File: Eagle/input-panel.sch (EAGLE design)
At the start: 23 parts, among them J1 UJC-HP-3-SMT-TR

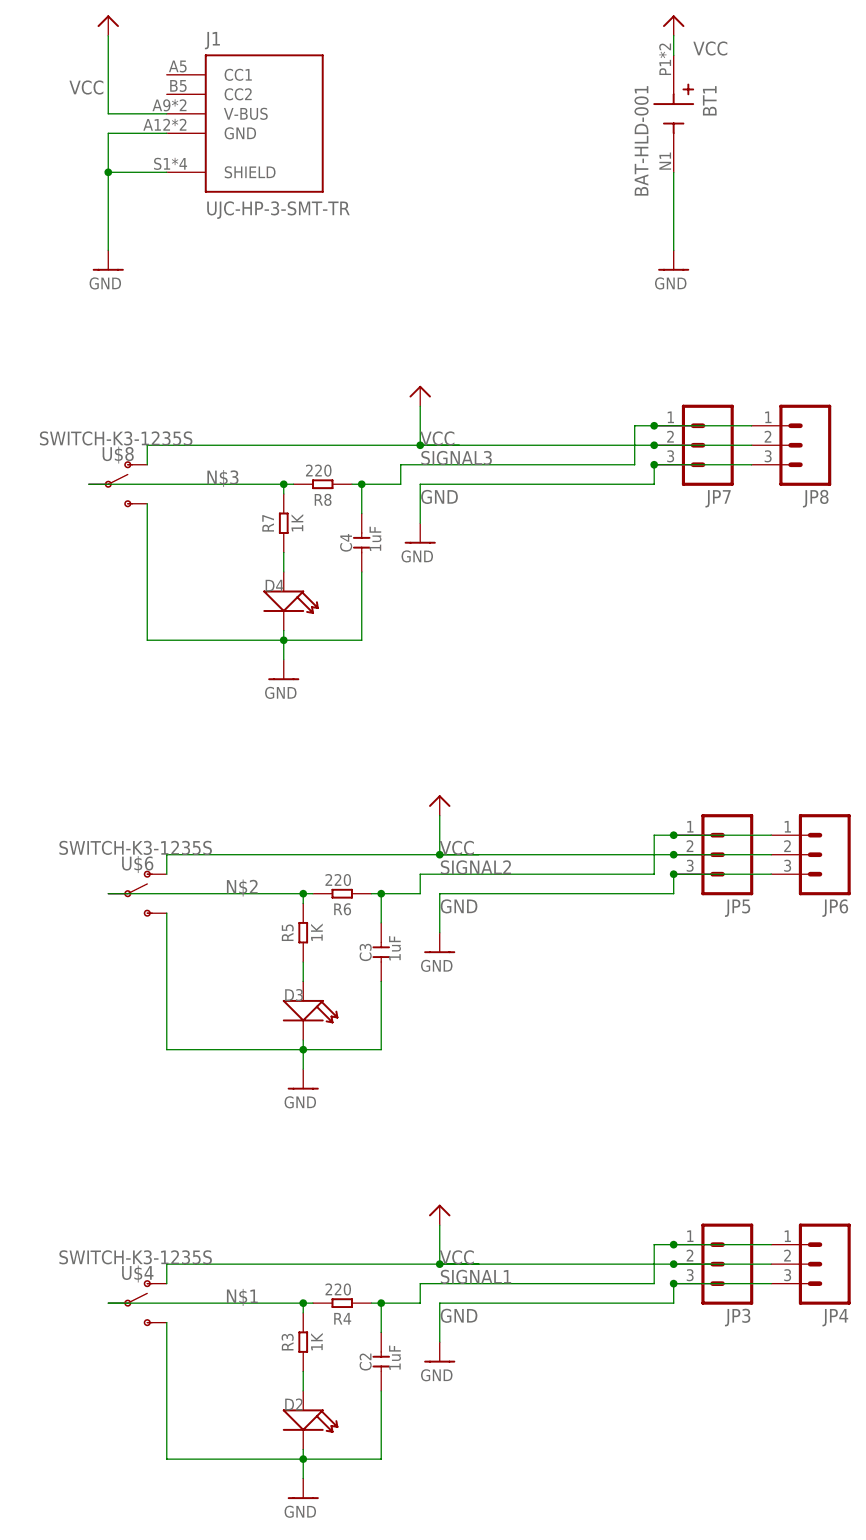
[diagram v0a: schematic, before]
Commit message: updated input panel
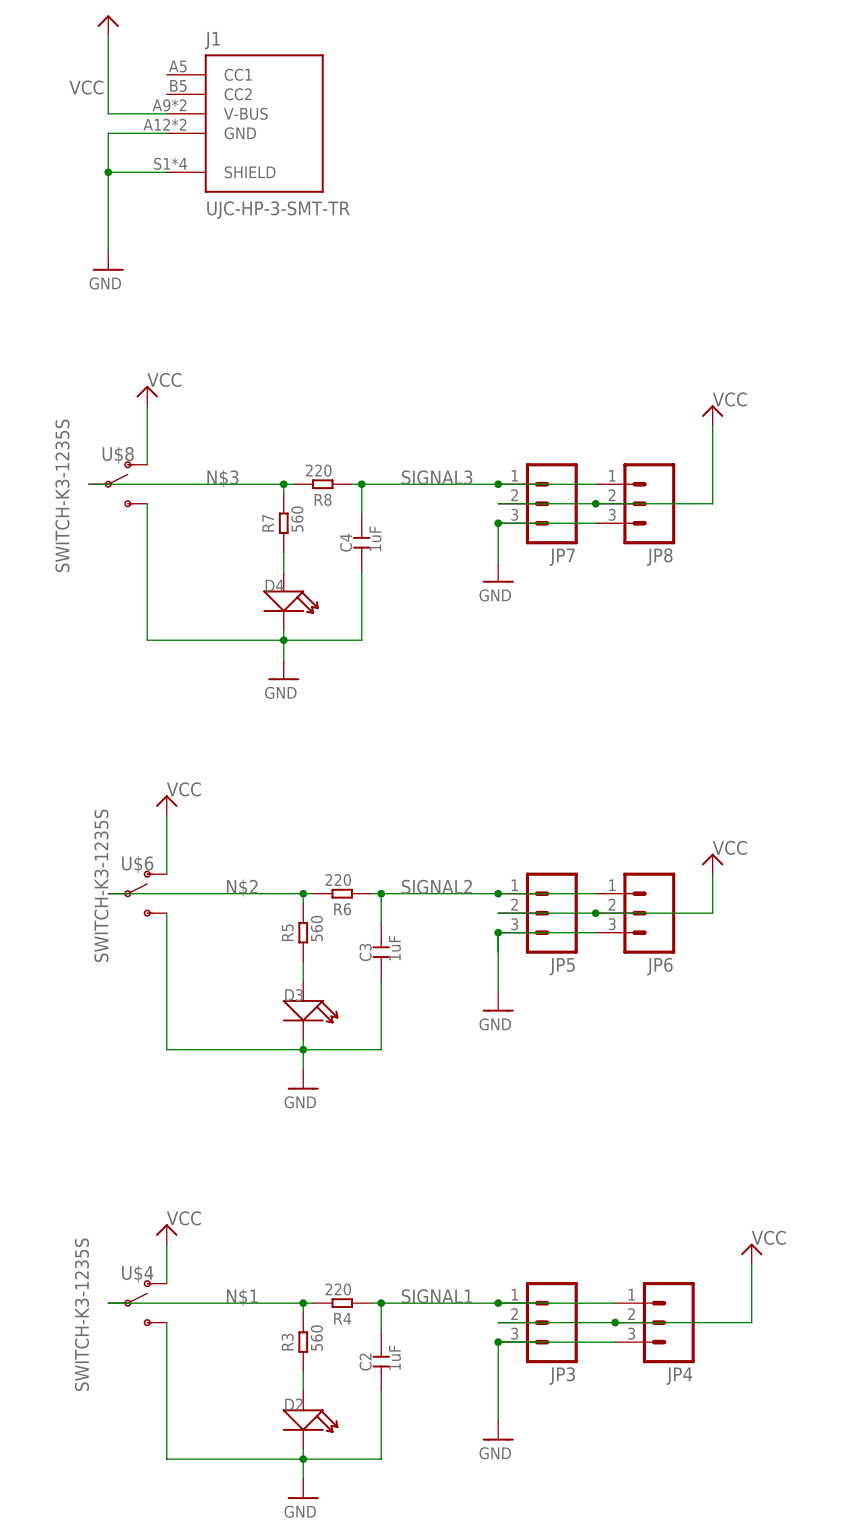
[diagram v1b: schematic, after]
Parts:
- removed BT1: BAT-HLD-001, BAT-HLD-001:BAT-HLD-001
- R3, R5, R7: value 1K -> 560
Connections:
- net GND: no longer BT1.-
- net VCC: no longer BT1.+
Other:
- moved on the sheet: JP3, JP4, JP5, JP6, JP7, JP8

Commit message: updated for v1.3
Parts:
- removed C4: 1uF, RoverWing-V1.5:CAP-CERAMIC-SMD0603
- removed R7: 560, RoverWing-V1.5:RES-SMD-0603
- removed R8: 220, RoverWing-V1.5:RES-SMD-0603
- added C1: 1uF, RoverWing-V1.5:CAP-CERAMIC-SMD0603
- added R1: 560, RoverWing-V1.5:RES-SMD-0603
- added R2: 220, RoverWing-V1.5:RES-SMD-0603
- JP3, JP4, JP5, JP6, JP7, JP8: device logicBlocks-AND-v12:SPARKFUN-CONNECTORS_M03SMD_RA_MALE -> logicBlocks-AND-v12:SPARKFUN_M031SMD-RA-MALE
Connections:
- net GND: now also C1.1; no longer C4.1
- net N$1: now also R1.2, R2.2; no longer R3.2, R4.2
- net N$2: now also R3.2, R4.2; no longer R5.2, R6.2
- net N$3: now also R5.2, R6.2; no longer R7.2, R8.2
- net N$4: now also R3.1; no longer R5.1
- net N$5: now also R1.1; no longer R3.1
- net N$6: now also R5.1; no longer R7.1
- net SIGNAL1: now also C1.2, R2.1; no longer C2.2, R4.1
- net SIGNAL2: now also C2.2, R4.1; no longer C3.2, R6.1
- net SIGNAL3: now also C3.2, R6.1; no longer C4.2, R8.1
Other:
- moved on the sheet: C2, C3, R3, R4, R5, R6
